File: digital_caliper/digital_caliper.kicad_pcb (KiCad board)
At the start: 2 copper layers, 13 parts, among them J1 Conn_01x05, J2 Conn_01x04_Male, Q1 2N3904, Q2 2N7000, Q3 2N7000, Q4 2N3904, Q5 2N3904

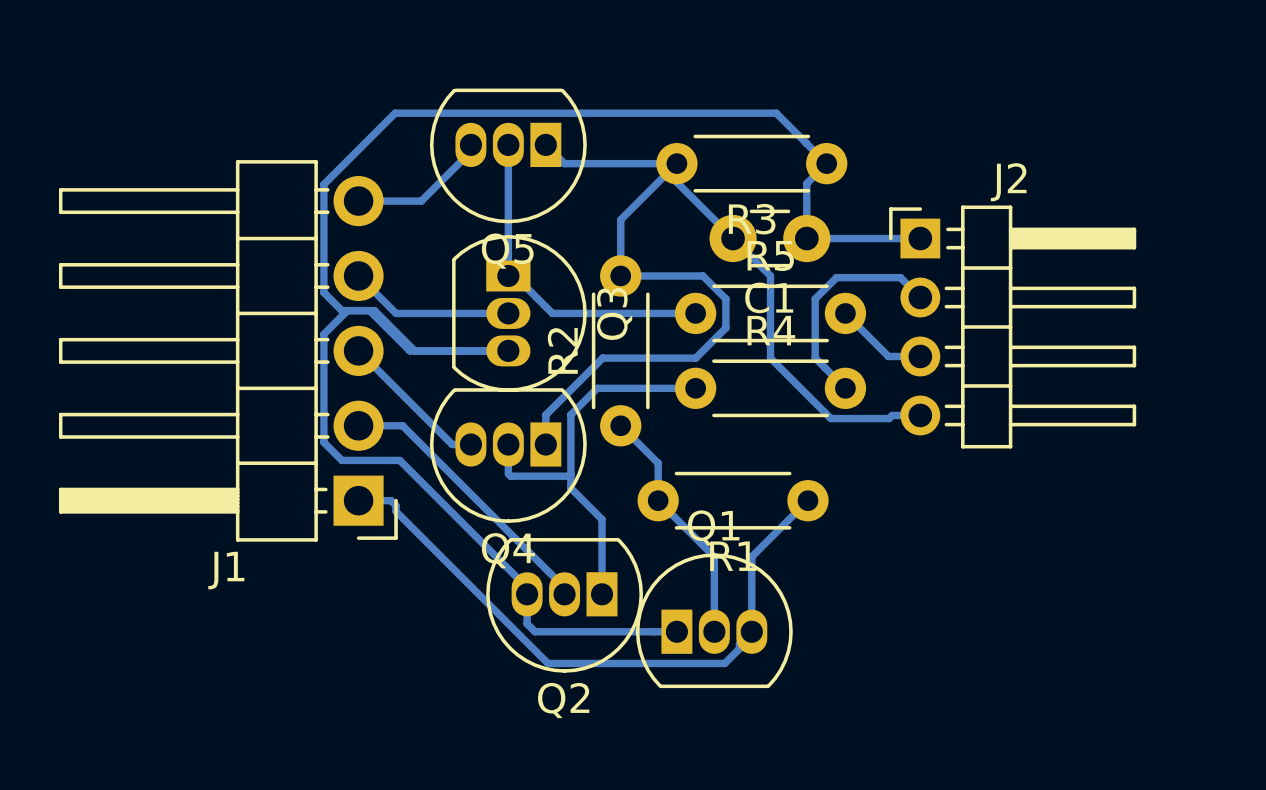
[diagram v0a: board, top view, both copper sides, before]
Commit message: Added FAULT line to force fast decay
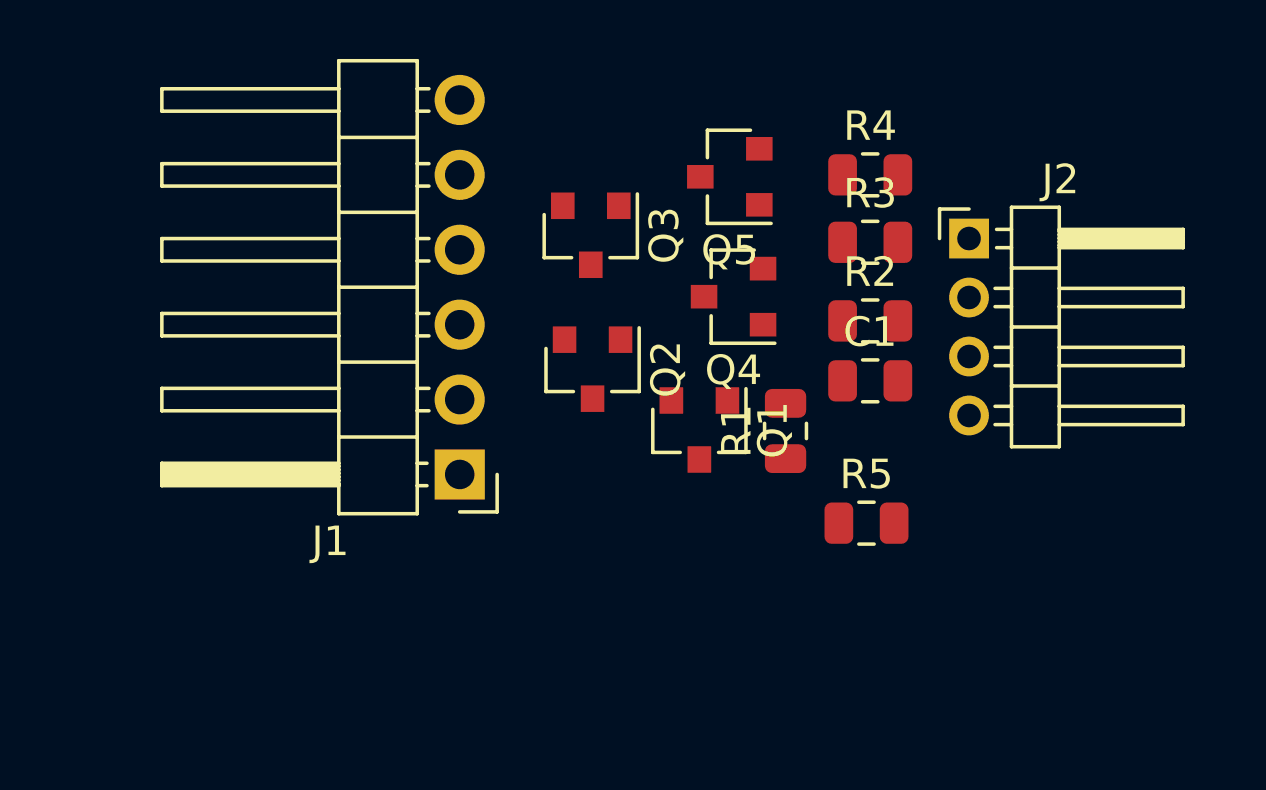
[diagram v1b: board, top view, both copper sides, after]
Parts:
- C1: footprint Capacitor_THT:C_Disc_D3.0mm_W1.6mm_P2.50mm -> Capacitor_SMD:C_0805_2012Metric
- J1: value Conn_01x05 -> Conn_01x06; footprint Connector_PinHeader_2.54mm:PinHeader_1x05_P2.54mm_Horizontal -> Connector_PinHeader_2.54mm:PinHeader_1x06_P2.54mm_Horizontal
- Q1, Q2, Q3, Q4, Q5: footprint Package_TO_SOT_THT:TO-92_Inline -> Package_TO_SOT_SMD:SOT-23
- R1, R2, R3, R4, R5: footprint Resistor_THT:R_Axial_DIN0204_L3.6mm_D1.6mm_P5.08mm_Horizontal -> Resistor_SMD:R_0805_2012Metric
- moved R4 9.35 mm to (92.9, 30.2)
- moved R2 9.18 mm to (92.9, 35.2), turned to 0 degrees
- moved R5 9.17 mm to (92.8, 42.0)
- moved Q4 8.10 mm to (88.3, 34.4)
- moved Q2 7.64 mm to (83.5, 36.8), turned to 270 degrees
- moved Q1 6.88 mm to (87.1, 38.9), turned to 270 degrees
- moved Q5 6.33 mm to (88.2, 30.3)
- moved C1 5.28 mm to (92.9, 37.2), turned to 0 degrees
- moved J1 3.54 mm to (79.0, 40.4)
- moved Q3 3.12 mm to (83.4, 32.3)
- moved R3 3.05 mm to (92.9, 32.5), turned to 0 degrees
- moved R1 2.48 mm to (90.0, 38.9), turned to 90 degrees
- moved J2 1.65 mm to (96.3, 32.4)
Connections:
- J1 pad 2: Net-(J1-Pad2) -> GNDREF
- Q2 pad 1: Net-(Q2-Pad1) -> Net-(J2-Pad2)
- Q2 pad 2: Net-(J1-Pad2) -> Net-(J1-Pad3)
- Q3 pad 1: Net-(Q3-Pad1) -> Net-(J2-Pad3)
- Q3 pad 2: Net-(J1-Pad4) -> Net-(J1-Pad5)
- Q4 pad 2: Net-(Q2-Pad1) -> Net-(Q4-Pad2)
- Q4 pad 3: Net-(J1-Pad3) -> Net-(J1-Pad4)
- Q5 pad 2: Net-(Q3-Pad1) -> Net-(Q5-Pad2)
- Q5 pad 3: Net-(J1-Pad5) -> Net-(J1-Pad6)
- R4 pad 1: Net-(Q2-Pad1) -> Net-(Q4-Pad2)
- R5 pad 1: Net-(Q3-Pad1) -> Net-(Q5-Pad2)
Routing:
- net Net-(C1-Pad1): track 62.3 -> 0.00 mm
- net GNDREF: track 36.4 -> 0.00 mm
- net Net-(J1-Pad1): track 21.5 -> 0.00 mm
- net Net-(Q2-Pad1): track 14.3 -> 0.00 mm
- net Net-(Q3-Pad1): track 11.3 -> 0.00 mm
- net Net-(J1-Pad2): track 9.48 -> 0.00 mm
- net Net-(Q1-Pad2): track 8.30 -> 0.00 mm
- net Net-(J2-Pad2): track 7.60 -> 0.00 mm
- net Net-(J1-Pad4): track 5.61 -> 0.00 mm
- net Net-(J1-Pad3): track 5.13 -> 0.00 mm
- net Net-(J1-Pad5): track 4.73 -> 0.00 mm
- net Net-(J2-Pad3): track 3.14 -> 0.00 mm
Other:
- net class Default: trace_width 0.25 -> 0.2
- rule trace_min: 0.2 -> 0.15

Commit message: Added Fourt Axis
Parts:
- C1: footprint Capacitor_SMD:C_0805_2012Metric -> Capacitor_SMD:C_1206_3216Metric
- R1, R2, R3, R4, R5: footprint Resistor_SMD:R_0805_2012Metric -> Resistor_SMD:R_1206_3216Metric
- moved R5 16.4 mm to (83.6, 28.4), turned to 180 degrees
- moved R4 4.96 mm to (92.6, 35.2)
- moved C1 4.58 mm to (92.7, 32.6), turned to 180 degrees
- moved Q1 3.54 mm to (83.7, 39.8)
- moved R2 3.23 mm to (92.3, 38.4)
- moved R3 3.19 mm to (92.6, 29.3), turned to 180 degrees
- moved R1 2.67 mm to (87.4, 39.1)
- moved J2 2.02 mm to (97.0, 30.5)
- moved Q2 0.76 mm to (83.5, 36.1)
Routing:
- net GNDREF: track 0.00 -> 32.6 mm, vias 0 -> 1
- net Net-(C1-Pad1): track 0.00 -> 30.7 mm
- net Net-(J2-Pad3): track 0.00 -> 17.7 mm, vias 0 -> 1
- net Net-(J2-Pad2): track 0.00 -> 15.1 mm, vias 0 -> 2
- net Net-(J1-Pad6): track 0.00 -> 10.0 mm
- net Net-(Q1-Pad2): track 0.00 -> 9.51 mm
- net Net-(J1-Pad4): track 0.00 -> 9.50 mm
- net Net-(J1-Pad1): track 0.00 -> 8.65 mm
- net Net-(Q5-Pad2): track 0.00 -> 4.91 mm
- net Net-(J1-Pad5): track 0.00 -> 3.96 mm
- net Net-(J1-Pad3): track 0.00 -> 3.67 mm
- net Net-(Q4-Pad2): track 0.00 -> 2.63 mm

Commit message: Added DRO
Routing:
- net Net-(Q1-Pad2): track 9.51 -> 10.7 mm
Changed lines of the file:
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@@
-(kicad_pcb (version 20171130) (host pcbnew 5.0.0-fee4fd1~66~ubuntu18.04.1)
+(kicad_pcb (version 20171130) (host pcbnew 5.0.0+dfsg1-2)
   (general
     (thickness 1.6)
     (drawings 0)
-    (tracks 97)
+    (tracks 98)
     (zones 0)
     (modules 13)
@@
   (segment (start 95.568 36.512) (end 93.726 38.354) (width 0.2) (layer F.Cu) (net 2))
   (segment (start 97.028 36.512) (end 95.568 36.512) (width 0.2) (layer F.Cu) (net 2))
-  (segment (start 89.331 35.306) (end 89.281 35.306) (width 0.2) (layer F.Cu) (net 2))
   (segment (start 92.55099 37.17899) (end 91.20399 37.17899) (width 0.2) (layer F.Cu) (net 2))
   (segment (start 93.726 38.354) (end 92.55099 37.17899) (width 0.2) (layer F.Cu) (net 2))
@@
   (segment (start 91.20399 37.17899) (end 90.805 36.78) (width 0.2) (layer F.Cu) (net 2))
   (segment (start 90.805 36.78) (end 89.331 35.306) (width 0.2) (layer F.Cu) (net 2))
-  (via (at 85.725 36.83) (size 0.8) (drill 0.4) (layers F.Cu B.Cu) (net 2))
-  (segment (start 86.098998 36.456002) (end 85.725 36.83) (width 0.2) (layer F.Cu) (net 2))
-  (segment (start 87.480998 36.456002) (end 86.098998 36.456002) (width 0.2) (layer F.Cu) (net 2))
+  (segment (start 89.331 35.306) (end 89.281 35.306) (width 0.2) (layer F.Cu) (net 2))
+  (segment (start 88.631 35.306) (end 87.488 36.449) (width 0.2) (layer F.Cu) (net 2))
   (segment (start 89.281 35.306) (end 88.631 35.306) (width 0.2) (layer F.Cu) (net 2))
-  (segment (start 88.631 35.306) (end 87.480998 36.456002) (width 0.2) (layer F.Cu) (net 2))
-  (segment (start 84.709 37.846) (end 78.994 37.846) (width 0.2) (layer B.Cu) (net 2))
-  (segment (start 85.725 36.83) (end 84.709 37.846) (width 0.2) (layer B.Cu) (net 2))
+  (segment (start 87.488 36.449) (end 86.4108 36.449) (width 0.2) (layer F.Cu) (net 2))
+  (via (at 85.852 37.7698) (size 0.8) (drill 0.4) (layers F.Cu B.Cu) (net 2))
+  (segment (start 86.4108 36.449) (end 85.852 37.0078) (width 0.2) (layer F.Cu) (net 2))
+  (segment (start 85.852 37.0078) (end 85.852 37.7698) (width 0.2) (layer F.Cu) (net 2))
+  (segment (start 79.0702 37.7698) (end 78.994 37.846) (width 0.2) (layer B.Cu) (net 2))
+  (segment (start 85.852 37.7698) (end 79.0702 37.7698) (width 0.2) (layer B.Cu) (net 2))
   (segment (start 94.361 35.179) (end 93.98 35.179) (width 0.2) (layer F.Cu) (net 3))
   (segment (start 97.028 32.512) (end 94.361 35.179) (width 0.2) (layer F.Cu) (net 3))
@@
   (segment (start 87.281 33.756) (end 86.048999 32.523999) (width 0.2) (layer F.Cu) (net 8))
   (segment (start 87.281 34.356) (end 87.281 33.756) (width 0.2) (layer F.Cu) (net 8))
-  (segment (start 86.68029 38.40871) (end 87.376 37.713) (width 0.2) (layer F.Cu) (net 9))
-  (segment (start 85.571999 39.517001) (end 86.68029 38.40871) (width 0.2) (layer F.Cu) (net 9))
-  (segment (start 84.093001 39.517001) (end 85.571999 39.517001) (width 0.2) (layer F.Cu) (net 9))
-  (segment (start 83.343 38.767) (end 84.093001 39.517001) (width 0.2) (layer F.Cu) (net 9))
-  (segment (start 82.743 38.767) (end 83.343 38.767) (width 0.2) (layer F.Cu) (net 9))
   (segment (start 90.285 37.713) (end 90.926 38.354) (width 0.2) (layer F.Cu) (net 9))
   (segment (start 87.376 37.713) (end 90.285 37.713) (width 0.2) (layer F.Cu) (net 9))
+  (segment (start 87.376 38.5064) (end 87.376 37.713) (width 0.2) (layer F.Cu) (net 9))
+  (segment (start 83.204 39.878) (end 86.0044 39.878) (width 0.2) (layer F.Cu) (net 9))
+  (segment (start 86.0044 39.878) (end 87.376 38.5064) (width 0.2) (layer F.Cu) (net 9))
+  (segment (start 82.743 38.767) (end 82.743 39.417) (width 0.2) (layer F.Cu) (net 9))
+  (segment (start 82.743 39.417) (end 83.204 39.878) (width 0.2) (layer F.Cu) (net 9))
   (segment (start 89.407 33.406) (end 89.281 33.406) (width 0.2) (layer F.Cu) (net 10))
   (segment (start 91.18 35.179) (end 89.407 33.406) (width 0.2) (layer F.Cu) (net 10))
